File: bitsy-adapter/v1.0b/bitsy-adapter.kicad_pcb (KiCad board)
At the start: 2 copper layers, 76 x 36 mm, 28 parts, among them J1 PMOD1, J2 PMOD2, J3 PMOD3, J4 5V AUX, J5 5V AUX

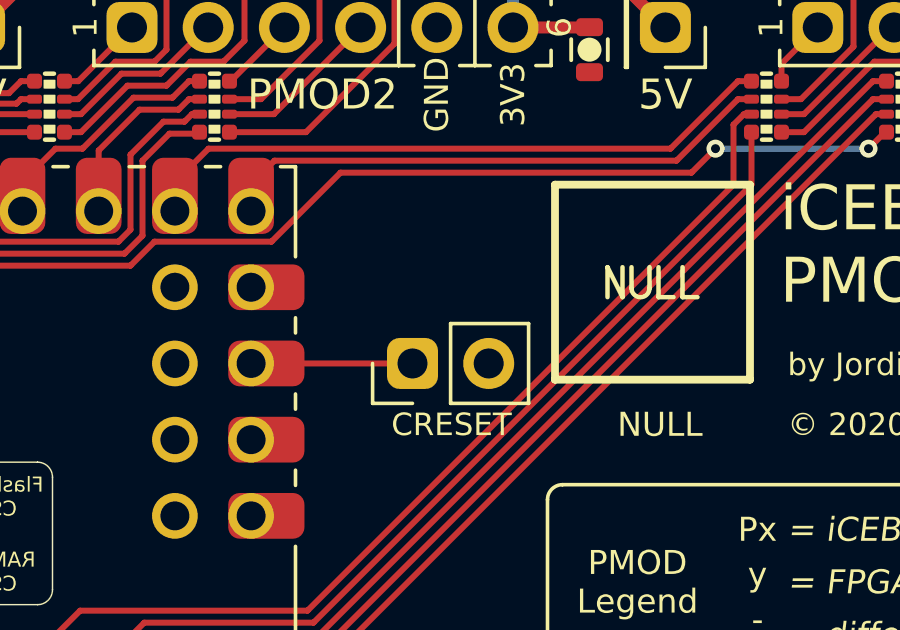
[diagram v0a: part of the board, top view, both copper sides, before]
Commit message: Bitsy adapter: finish v1.0b
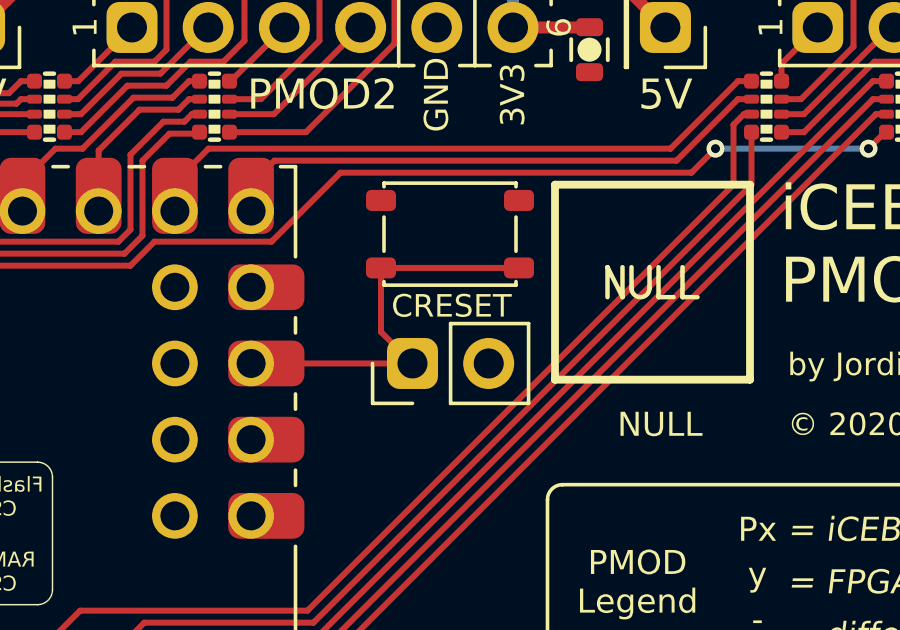
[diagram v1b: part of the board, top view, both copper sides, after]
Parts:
- added SW1: CRESET, pkl_buttons_switches:SW_SPST_3x4x2.5, F.Cu at (104.2, 93.2)
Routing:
- net /CRESET: track 5.38 -> 13.6 mm
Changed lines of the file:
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@@
     (thickness 1.6)
     (drawings 541)
-    (tracks 273)
+    (tracks 276)
     (zones 0)
-    (modules 28)
+    (modules 29)
     (nets 59)
   )
@@
   (title_block
     (title "iCEBreaker Bitsy PMOD Adapter")
-    (date 2020-11-23)
+    (date 2020-12-03)
     (rev v1.0b)
     (company 1BitSquared)
@@
       (effects (font (size 1 1) (thickness 0.15)) (justify mirror))
     )
-    (fp_arc (start -0.4 -0.2) (end -0.7 -0.2) (angle 180) (layer B.SilkS) (width 0.15))
     (fp_line (start 1 -0.5) (end 1.5 -0.5) (layer B.SilkS) (width 0.15))
     (fp_line (start 1 0.5) (end 1 -0.5) (layer B.SilkS) (width 0.15))
@@
     (fp_line (start 3.25 3.25) (end 3.25 -3.25) (layer B.SilkS) (width 0.26))
     (fp_line (start -3.25 -3.25) (end 3.25 -3.25) (layer B.SilkS) (width 0.26))
+    (fp_arc (start -0.4 -0.2) (end -0.7 -0.2) (angle 180) (layer B.SilkS) (width 0.15))
+  )
+  (module pkl_buttons_switches:SW_SPST_3x4x2.5 (layer F.Cu)
+    (at 104.25 93.15 180)
+    (descr "C&K Components, PTS 810 Series, Microminiature SMT Top Actuated, http://www.ckswitches.com/media/1476/pts810.pdf")
+    (tags "SPST Button Switch")
+    (attr smd)
+    (fp_text reference SW1 (at 0 -2.6) (layer F.Fab)
+      (effects (font (size 1 1) (thickness 0.15)))
+    )
+    (fp_text value CRESET (at 0 2.6) (layer F.Fab)
+      (effects (font (size 1 1) (thickness 0.15)))
+    )
+    (fp_line (start 2.1 1.6) (end 2.1 -1.6) (layer F.Fab) (width 0.1))
+    (fp_line (start 2.1 -1.6) (end -2.1 -1.6) (layer F.Fab) (width 0.1))
+    (fp_line (start -2.1 -1.6) (end -2.1 1.6) (layer F.Fab) (width 0.1))
+    (fp_line (start -2.1 1.6) (end 2.1 1.6) (layer F.Fab) (width 0.1))
+    (fp_line (start -0.4 -1.1) (end 0.4 -1.1) (layer F.Fab) (width 0.1))
+    (fp_line (start 0.4 1.1) (end -0.4 1.1) (layer F.Fab) (width 0.1))
+    (fp_line (start 2.2 -1.7) (end -2.2 -1.7) (layer F.SilkS) (width 0.12))
+    (fp_line (start -2.2 -1.7) (end -2.2 -1.58) (layer F.SilkS) (width 0.12))
+    (fp_line (start -2.2 -0.57) (end -2.2 0.57) (layer F.SilkS) (width 0.12))
+    (fp_line (start -2.2 1.58) (end -2.2 1.7) (layer F.SilkS) (width 0.12))
+    (fp_line (start -2.2 1.7) (end 2.2 1.7) (layer F.SilkS) (width 0.12))
+    (fp_line (start 2.2 1.7) (end 2.2 1.58) (layer F.SilkS) (width 0.12))
+    (fp_line (start 2.2 0.57) (end 2.2 -0.57) (layer F.SilkS) (width 0.12))
+    (fp_line (start 2.2 -1.58) (end 2.2 -1.7) (layer F.SilkS) (width 0.12))
+    (fp_line (start 3.05 -1.85) (end 3.05 1.85) (layer F.CrtYd) (width 0.05))
+    (fp_line (start 3.05 1.85) (end -3.05 1.85) (layer F.CrtYd) (width 0.05))
+    (fp_line (start -3.05 1.85) (end -3.05 -1.85) (layer F.CrtYd) (width 0.05))
+    (fp_line (start -3.05 -1.85) (end 3.05 -1.85) (layer F.CrtYd) (width 0.05))
+    (fp_arc (start 0.4 0) (end 0.4 -1.1) (angle 180) (layer F.Fab) (width 0.1))
+    (fp_arc (start -0.4 0) (end -0.4 1.1) (angle 180) (layer F.Fab) (width 0.1))
+    (pad 2 smd roundrect (at 2.3 1.125 180) (size 1 0.7) (layers F.Cu F.Paste F.Mask) (roundrect_rratio 0.25)
+      (net 2 GND))
+    (pad 2 smd roundrect (at -2.3 1.125 180) (size 1 0.7) (layers F.Cu F.Paste F.Mask) (roundrect_rratio 0.25)
+      (net 2 GND))
+    (pad 1 smd roundrect (at 2.3 -1.125 180) (size 1 0.7) (layers F.Cu F.Paste F.Mask) (roundrect_rratio 0.25)
+      (net 52 /CRESET))
+    (pad 1 smd roundrect (at -2.3 -1.125 180) (size 1 0.7) (layers F.Cu F.Paste F.Mask) (roundrect_rratio 0.25)
+      (net 52 /CRESET))
+    (model ${KISYS3DMOD}/Button_Switch_SMD.3dshapes/SW_SPST_PTS810.wrl
+      (at (xyz 0 0 0))
+      (scale (xyz 1 1 1))
+      (rotate (xyz 0 0 0))
+    )
+    (model ${KIPRJMOD}/../../lib/pkl/packages3d/pkl_buttons_switches.3dshapes/PTS810SJG250SMTRLFS.step
+      (offset (xyz 0 0 1.45))
+      (scale (xyz 1 1 1))
+      (rotate (xyz -90 0 0))
+    )
   )
   (module pkl_module:iCEBreaker_Bitsy (layer F.Cu)
@@
     (effects (font (size 0.8 0.8) (thickness 0.12)))
   )
-  (gr_text CRESET (at 104.3 99.5) (layer F.SilkS)
+  (gr_text CRESET (at 104.3 95.55) (layer F.SilkS)
     (effects (font (size 0.75 0.75) (thickness 0.12)))
   )
@@
   (segment (start 115.3 88.05) (end 115.3 87.47) (width 0.2) (layer F.Cu) (net 51))
   (segment (start 103 97.46) (end 97.62 97.46) (width 0.2) (layer F.Cu) (net 52))
+  (segment (start 106.55 94.275) (end 101.95 94.275) (width 0.2) (layer F.Cu) (net 52))
+  (segment (start 101.95 96.41) (end 103 97.46) (width 0.2) (layer F.Cu) (net 52))
+  (segment (start 101.95 94.275) (end 101.95 96.41) (width 0.2) (layer F.Cu) (net 52))
   (zone (net 2) (net_name GND) (layer F.Cu) (hatch edge 0.508)
     (connect_pads (clearance 0.2))
